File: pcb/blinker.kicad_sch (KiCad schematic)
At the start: 14 parts, among them J1 ISP, U1 ATtiny10-TS

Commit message: About to route PCB.
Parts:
- D2: footprint Diode_SMD:D_SOD-123 -> Diode_SMD:D_SOD-123F; LCSC C707156 -> C362294
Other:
- note removed: "Check connector orientation"
- note removed: "More?"
- moved on the sheet: D3, J1, JP1, R1

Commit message: Routed
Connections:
- net LED_R: now reaches D3.1 (K), R1.2
- net SLR_IN: now reaches D1.2 (A), SC1.1 (+)
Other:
- moved on the sheet: R1
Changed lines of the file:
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@@
     (stroke (width 0) (type default) (color 0 0 0 0))
   )
-  (wire (pts (xy 59.69 119.38) (xy 59.69 123.19))
+  (wire (pts (xy 59.69 121.92) (xy 59.69 125.73))
     (stroke (width 0) (type default) (color 0 0 0 0))
   )
@@
     (stroke (width 0) (type default) (color 0 0 0 0))
   )
+  (wire (pts (xy 59.69 114.3) (xy 59.69 111.76))
+    (stroke (width 0) (type default) (color 0 0 0 0))
+  )
   (wire (pts (xy 137.16 80.01) (xy 146.05 80.01))
     (stroke (width 0) (type default) (color 0 0 0 0))
@@
   (wire (pts (xy 101.6 62.23) (xy 110.49 62.23))
     (stroke (width 0) (type default) (color 0 0 0 0))
+  )
+  (label "LED_R" (at 59.69 113.03 180)
+    (effects (font (size 1.27 1.27)) (justify right bottom))
+  )
+  (label "SLR_IN" (at 63.5 62.23 180)
+    (effects (font (size 1.27 1.27)) (justify right bottom))
   )
   (global_label "TPICLK" (shape input) (at 140.97 109.22 180) (fields_autoplaced)
@@
     )
   )
-  (global_label "LED" (shape input) (at 59.69 123.19 270) (fields_autoplaced)
+  (global_label "LED" (shape input) (at 59.69 125.73 270) (fields_autoplaced)
     (effects (font (size 1.27 1.27)) (justify right))
-    (property "Intersheet References" "${INTERSHEET_REFS}" (id 0) (at 59.7694 129.0502 90)
+    (property "Intersheet References" "${INTERSHEET_REFS}" (id 0) (at 59.7694 131.5902 90)
       (effects (font (size 1.27 1.27)) (justify right) hide)
     )
   )
-  (symbol (lib_id "Device:R") (at 59.69 115.57 180) (unit 1)
+  (symbol (lib_id "Device:R") (at 59.69 118.11 180) (unit 1)
     (in_bom yes) (on_board yes)
-    (property "Reference" "R1" (id 0) (at 61.468 113.2739 0)
+    (property "Reference" "R1" (id 0) (at 61.468 115.8139 0)
       (effects (font (size 1.27 1.27)) (justify right))
     )
-    (property "Value" "220" (id 1) (at 61.468 116.049 0)
+    (property "Value" "220" (id 1) (at 61.468 118.589 0)
       (effects (font (size 1.27 1.27)) (justify right))
     )
-    (property "Footprint" "Resistor_SMD:R_0603_1608Metric" (id 2) (at 53.34 129.54 90)
+    (property "Footprint" "Resistor_SMD:R_0603_1608Metric" (id 2) (at 68.58 133.35 90)
       (effects (font (size 1.27 1.27)) (justify right))
     )
-    (property "Datasheet" "~" (id 3) (at 59.69 115.57 0)
+    (property "Datasheet" "~" (id 3) (at 59.69 118.11 0)
       (effects (font (size 1.27 1.27)) hide)
     )
-    (property "JLC" "C22962" (id 4) (at 59.69 115.57 0)
+    (property "JLC" "C22962" (id 4) (at 59.69 118.11 0)
       (effects (font (size 1.27 1.27)) hide)
     )

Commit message: Fix zener selection.
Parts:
- D2: footprint Diode_SMD:D_SOD-123F -> Diode_SMD:D_SOD-123; LCSC C362294 -> C96629
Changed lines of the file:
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@@
       (effects (font (size 1.27 1.27)) (justify left))
     )
-    (property "Footprint" "Diode_SMD:D_SOD-123F" (id 2) (at 83.82 72.39 0)
+    (property "Footprint" "Diode_SMD:D_SOD-123" (id 2) (at 83.82 72.39 0)
       (effects (font (size 1.27 1.27)) hide)
     )
@@
       (effects (font (size 1.27 1.27)) hide)
     )
-    (property "LCSC" "C362294" (id 4) (at 83.82 72.39 90)
+    (property "LCSC" "C96629" (id 4) (at 83.82 72.39 90)
       (effects (font (size 1.27 1.27)) hide)
     )
@@
     )
     (path "/edc8f391-0b6a-4a66-802b-2b3733d943db"
-      (reference "D2") (unit 1) (value "D_Zener") (footprint "Diode_SMD:D_SOD-123F")
+      (reference "D2") (unit 1) (value "D_Zener") (footprint "Diode_SMD:D_SOD-123")
     )
     (path "/d48d21e9-26d7-4a5d-9b01-cee4f624edbc"

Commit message: v1.0 PCB
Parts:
- D3: footprint LED_SMD:LED_0805_2012Metric -> LED_SMD:LED_0603_1608Metric; LCSC C84256 -> C2286
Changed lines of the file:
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@@
       (effects (font (size 1.27 1.27)) (justify right))
     )
-    (property "Footprint" "LED_SMD:LED_0805_2012Metric" (id 2) (at 59.69 107.95 0)
+    (property "Footprint" "LED_SMD:LED_0603_1608Metric" (id 2) (at 59.69 107.95 0)
       (effects (font (size 1.27 1.27)) hide)
     )
@@
       (effects (font (size 1.27 1.27)) hide)
     )
-    (property "LCSC" "C84256" (id 4) (at 59.69 107.95 90)
+    (property "LCSC" "C2286" (id 4) (at 59.69 107.95 90)
       (effects (font (size 1.27 1.27)) hide)
     )
@@
     )
     (path "/d48d21e9-26d7-4a5d-9b01-cee4f624edbc"
-      (reference "D3") (unit 1) (value "LED") (footprint "LED_SMD:LED_0805_2012Metric")
+      (reference "D3") (unit 1) (value "LED") (footprint "LED_SMD:LED_0603_1608Metric")
     )
     (path "/502b5450-a9f9-4289-a2e5-6125591610ce"

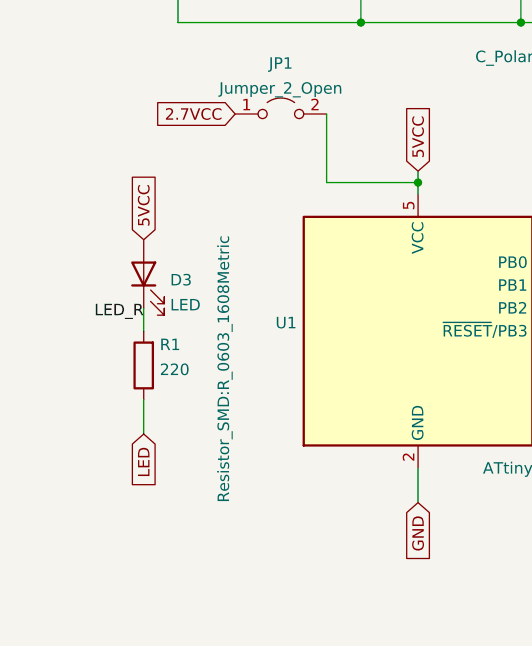
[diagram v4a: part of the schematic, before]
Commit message: Add through-hole pads for external LED. Reduce thermal relief spoke thickness on fill zones to 0.01 in
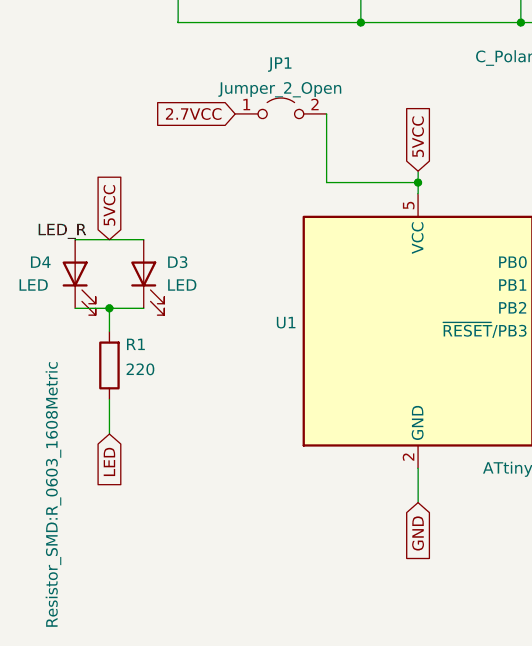
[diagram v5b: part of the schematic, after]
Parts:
- added D4: LED, Connector_PinHeader_2.54mm:PinHeader_1x02_P2.54mm_Vertical, symbol Device:LED
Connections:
- net 5VCC: now also D4.2 (A)
- net LED_R: no longer names the net of D3.1 (K), R1.2
- net LED_R: now also D4.1 (K)
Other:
- moved on the sheet: R1
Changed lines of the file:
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@@
   (junction (at 101.6 80.01) (diameter 0) (color 0 0 0 0)
   )
+  (junction (at 55.88 111.76) (diameter 0) (color 0 0 0 0)
+  )
   (junction (at 83.82 62.23) (diameter 0) (color 0 0 0 0)
   )
@@
     (stroke (width 0) (type default) (color 0 0 0 0))
   )
+  (wire (pts (xy 55.88 111.76) (xy 59.69 111.76))
+    (stroke (width 0) (type default) (color 0 0 0 0))
+  )
   (wire (pts (xy 101.6 76.2) (xy 101.6 80.01))
     (stroke (width 0) (type default) (color 0 0 0 0))
@@
     (stroke (width 0) (type default) (color 0 0 0 0))
   )
-  (wire (pts (xy 59.69 121.92) (xy 59.69 125.73))
+  (wire (pts (xy 52.07 111.76) (xy 55.88 111.76))
+    (stroke (width 0) (type default) (color 0 0 0 0))
+  )
+  (wire (pts (xy 55.88 121.92) (xy 55.88 125.73))
     (stroke (width 0) (type default) (color 0 0 0 0))
   )
@@
     (stroke (width 0) (type default) (color 0 0 0 0))
   )
+  (wire (pts (xy 52.07 104.14) (xy 59.69 104.14))
+    (stroke (width 0) (type default) (color 0 0 0 0))
+  )
   (wire (pts (xy 63.5 62.23) (xy 68.58 62.23))
     (stroke (width 0) (type default) (color 0 0 0 0))
@@
     (stroke (width 0) (type default) (color 0 0 0 0))
   )
-  (wire (pts (xy 59.69 114.3) (xy 59.69 111.76))
+  (wire (pts (xy 55.88 111.76) (xy 55.88 114.3))
     (stroke (width 0) (type default) (color 0 0 0 0))
   )
@@
     (stroke (width 0) (type default) (color 0 0 0 0))
   )
-  (label "LED_R" (at 59.69 113.03 180)
+  (label "LED_R" (at 53.34 104.14 180)
     (effects (font (size 1.27 1.27)) (justify right bottom))
   )
@@
     )
   )
-  (global_label "5VCC" (shape input) (at 59.69 104.14 90) (fields_autoplaced)
-    (effects (font (size 1.27 1.27)) (justify left))
-    (property "Intersheet References" "${INTERSHEET_REFS}" (id 0) (at 59.6106 96.8888 90)
+  (global_label "5VCC" (shape input) (at 55.88 104.14 90) (fields_autoplaced)
+    (effects (font (size 1.27 1.27)) (justify left))
+    (property "Intersheet References" "${INTERSHEET_REFS}" (id 0) (at 55.8006 96.8888 90)
       (effects (font (size 1.27 1.27)) (justify left) hide)
     )
@@
     )
   )
-  (global_label "LED" (shape input) (at 59.69 125.73 270) (fields_autoplaced)
+  (global_label "LED" (shape input) (at 55.88 125.73 270) (fields_autoplaced)
     (effects (font (size 1.27 1.27)) (justify right))
-    (property "Intersheet References" "${INTERSHEET_REFS}" (id 0) (at 59.7694 131.5902 90)
+    (property "Intersheet References" "${INTERSHEET_REFS}" (id 0) (at 55.9594 131.5902 90)
       (effects (font (size 1.27 1.27)) (justify right) hide)
     )
   )
-  (symbol (lib_id "Device:R") (at 59.69 118.11 180) (unit 1)
-    (in_bom yes) (on_board yes)
-    (property "Reference" "R1" (id 0) (at 61.468 115.8139 0)
-      (effects (font (size 1.27 1.27)) (justify right))
-    )
-    (property "Value" "220" (id 1) (at 61.468 118.589 0)
-      (effects (font (size 1.27 1.27)) (justify right))
-    )
-    (property "Footprint" "Resistor_SMD:R_0603_1608Metric" (id 2) (at 68.58 133.35 90)
-      (effects (font (size 1.27 1.27)) (justify right))
-    )
-    (property "Datasheet" "~" (id 3) (at 59.69 118.11 0)
-      (effects (font (size 1.27 1.27)) hide)
-    )
-    (property "JLC" "C22962" (id 4) (at 59.69 118.11 0)
+  (symbol (lib_id "Device:R") (at 55.88 118.11 180) (unit 1)
+    (in_bom yes) (on_board yes)
+    (property "Reference" "R1" (id 0) (at 57.658 115.8139 0)
+      (effects (font (size 1.27 1.27)) (justify right))
+    )
+    (property "Value" "220" (id 1) (at 57.658 118.589 0)
+      (effects (font (size 1.27 1.27)) (justify right))
+    )
+    (property "Footprint" "Resistor_SMD:R_0603_1608Metric" (id 2) (at 49.53 147.32 90)
+      (effects (font (size 1.27 1.27)) (justify right))
+    )
+    (property "Datasheet" "~" (id 3) (at 55.88 118.11 0)
+      (effects (font (size 1.27 1.27)) hide)
+    )
+    (property "JLC" "C22962" (id 4) (at 55.88 118.11 0)
       (effects (font (size 1.27 1.27)) hide)
     )
@@
     (pin "2")
   )
+  (symbol (lib_id "Device:LED") (at 52.07 107.95 90) (unit 1)
+    (in_bom yes) (on_board yes)
+    (property "Reference" "D4" (id 0) (at 46.99 106.68 90)
+      (effects (font (size 1.27 1.27)) (justify right))
+    )
+    (property "Value" "LED" (id 1) (at 45.72 109.22 90)
+      (effects (font (size 1.27 1.27)) (justify right))
+    )
+    (property "Footprint" "Connector_PinHeader_2.54mm:PinHeader_1x02_P2.54mm_Vertical" (id 2) (at 52.07 107.95 0)
+      (effects (font (size 1.27 1.27)) hide)
+    )
+    (property "Datasheet" "~" (id 3) (at 52.07 107.95 0)
+      (effects (font (size 1.27 1.27)) hide)
+    )
+    (pin "1")
+    (pin "2")
+  )
   (symbol (lib_id "Device:C_Polarized") (at 137.16 72.39 0) (unit 1)
     (in_bom yes) (on_board yes)
@@
   )
   (symbol (lib_id "Device:LED") (at 59.69 107.95 90) (unit 1)
-    (in_bom yes) (on_board yes) (fields_autoplaced)
-    (property "Reference" "D3" (id 0) (at 62.611 108.629 90)
-      (effects (font (size 1.27 1.27)) (justify right))
-    )
-    (property "Value" "LED" (id 1) (at 62.611 111.4041 90)
+    (in_bom yes) (on_board yes)
+    (property "Reference" "D3" (id 0) (at 62.23 106.68 90)
+      (effects (font (size 1.27 1.27)) (justify right))
+    )
+    (property "Value" "LED" (id 1) (at 62.23 109.22 90)
       (effects (font (size 1.27 1.27)) (justify right))
     )
@@
       (reference "D3") (unit 1) (value "LED") (footprint "LED_SMD:LED_0603_1608Metric")
     )
+    (path "/71b25962-3bdb-41b6-8555-b03d1677ed65"
+      (reference "D4") (unit 1) (value "LED") (footprint "Connector_PinHeader_2.54mm:PinHeader_1x02_P2.54mm_Vertical")
+    )
     (path "/502b5450-a9f9-4289-a2e5-6125591610ce"

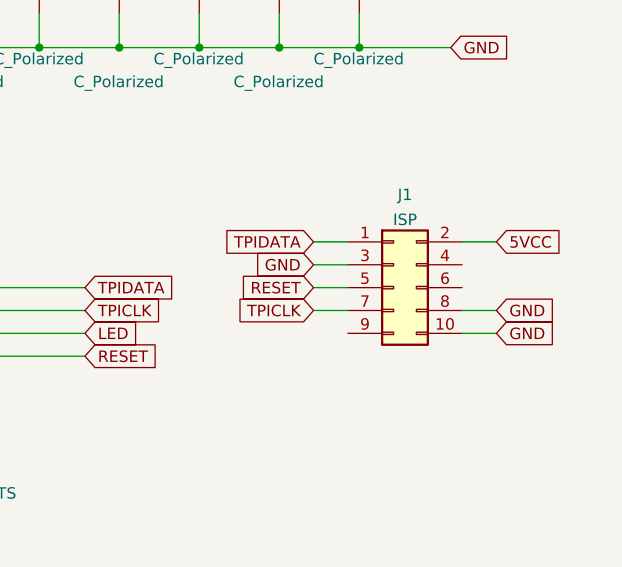
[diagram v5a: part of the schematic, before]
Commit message: Replace cap disconnect jumper with solder bridge.
Replace 10-pin AVRISP with 6-pad version.

Rearrangements
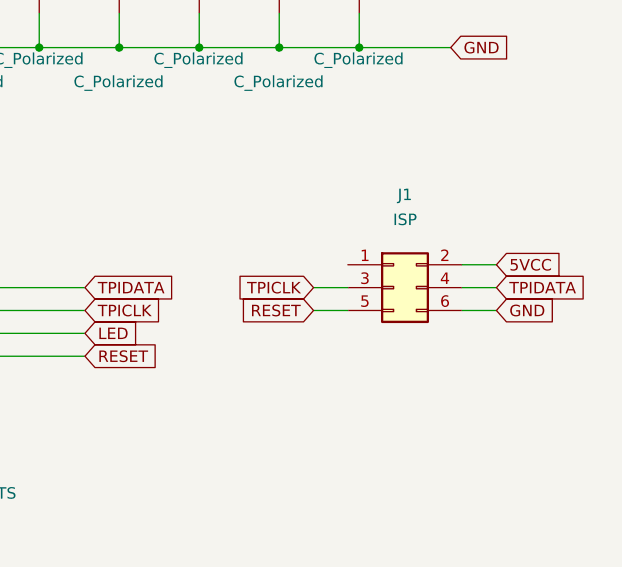
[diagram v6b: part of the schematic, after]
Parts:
- J1: footprint Connector_PinHeader_2.54mm:PinHeader_2x05_P2.54mm_Vertical -> Blinker:AVRISP_6PAD; symbol Connector_Generic:Conn_02x05_Odd_Even -> Connector_Generic:Conn_02x03_Odd_Even
- JP1: footprint Connector_PinHeader_2.54mm:PinHeader_1x02_P2.54mm_Vertical -> Jumper:SolderJumper-2_P1.3mm_Open_TrianglePad1.0x1.5mm
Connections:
- net GND: now also J1.6 (Pin_6); no longer J1.10 (Pin_10), J1.3 (Pin_3), J1.8 (Pin_8)
- net TPICLK: now also J1.3 (Pin_3); no longer J1.7 (Pin_7)
- net TPIDATA: now also J1.4 (Pin_4); no longer J1.1 (Pin_1)

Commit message: v1.2 of PCB
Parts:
- removed C1, C2, C3, C4: C_Polarized, Capacitor_THT:CP_Radial_D16.0mm_P7.50mm, symbol Device:C_Polarized
- removed D2: D_Zener, Diode_SMD:D_SOD-123, symbol Device:D_Zener
- removed D4: LED, Connector_PinHeader_2.54mm:PinHeader_1x02_P2.54mm_Vertical, symbol Device:LED
- renumbered C5 to C1, C6 to C2
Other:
- moved on the sheet: C1, C2, D3

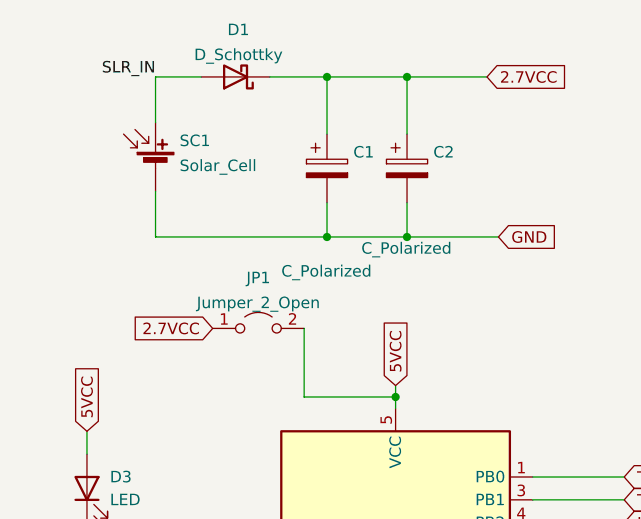
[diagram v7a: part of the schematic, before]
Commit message: Migrate to kicad 9
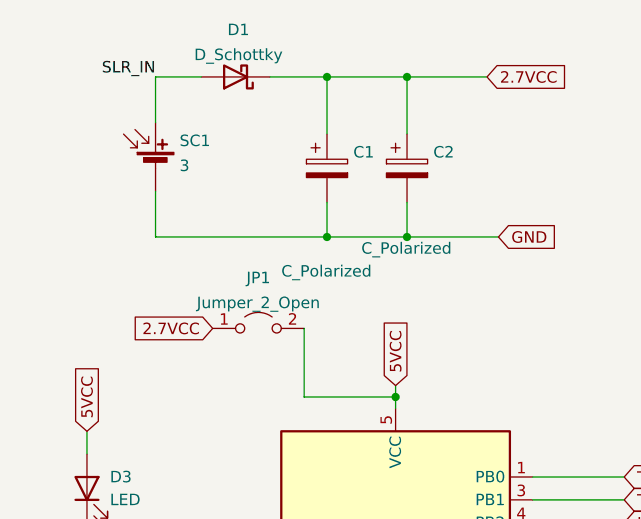
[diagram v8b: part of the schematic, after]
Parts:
- SC1: value Solar_Cell -> 3; Spice_Model dc 3 -> (none); Spice_Netlist_Enabled Y -> (none); Spice_Primitive I -> (none)
